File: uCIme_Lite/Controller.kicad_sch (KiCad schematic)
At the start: 36 parts, among them J11 SERIAL_MODE, J12 SERIAL_VOLTAGE_SELECT, Q5 BSS138, Q6 BSS138, Q7 BSS138, Q8 BSS138, U3 AP2204K-ADJ, U4 AP2204K-ADJ, U5 FT230XS, U6 TXB0104D

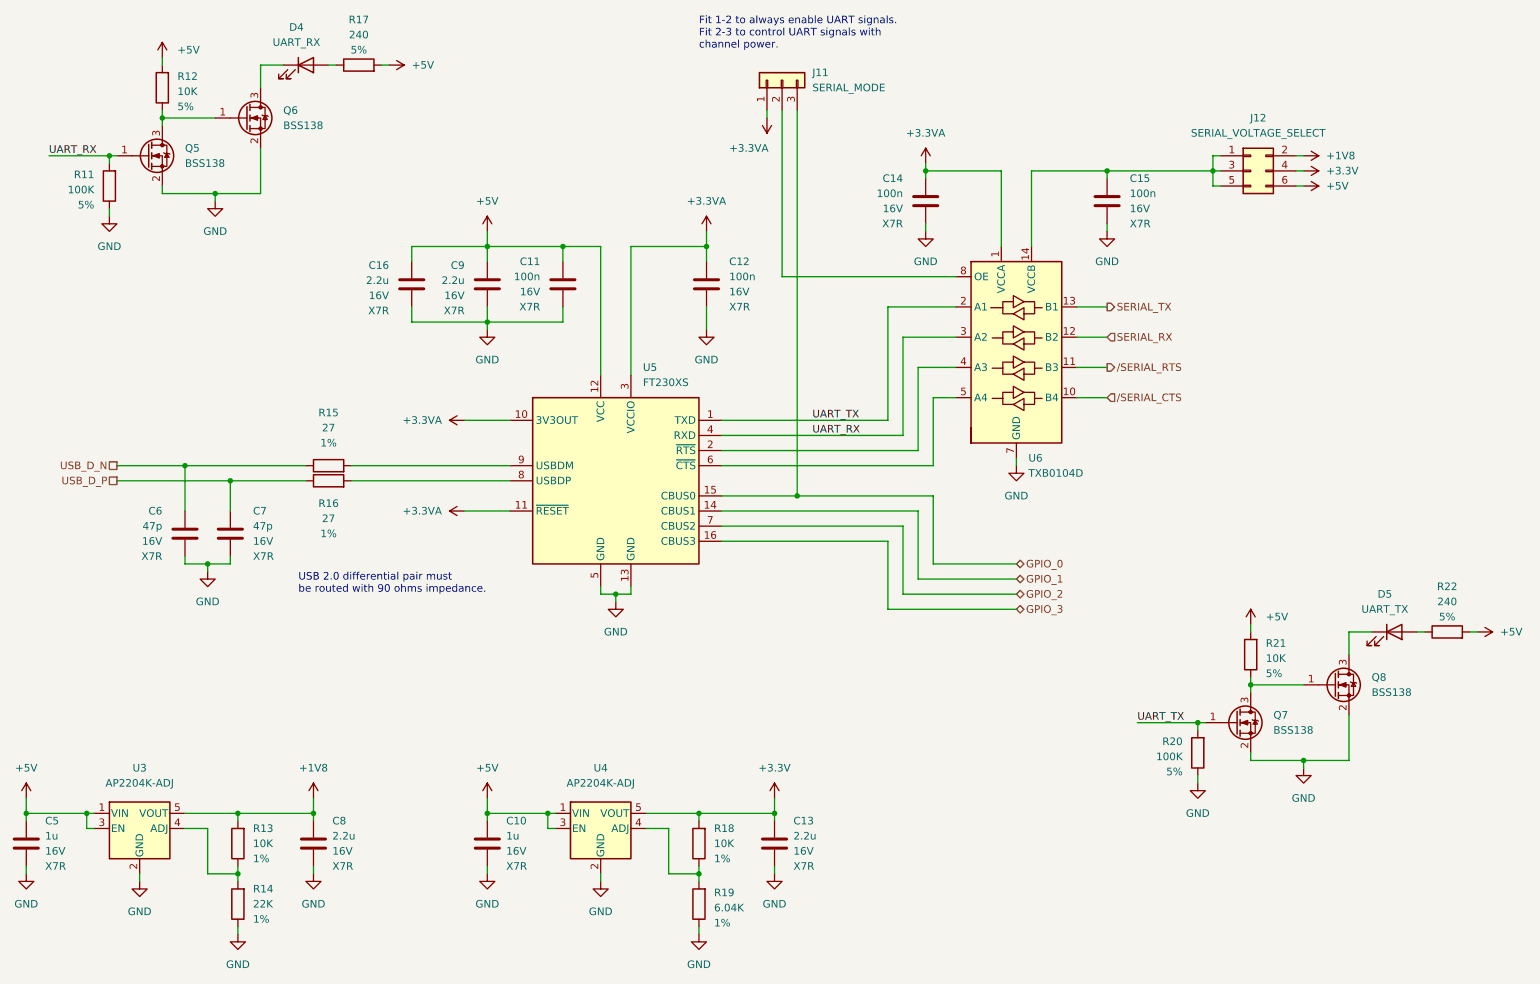
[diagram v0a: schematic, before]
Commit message: lite: Swapped UART RX and UART TX leds in schematic to ease PCB routing.
Signed-off-by: Adrien Ricciardi <aricciardi@baylibre.com>
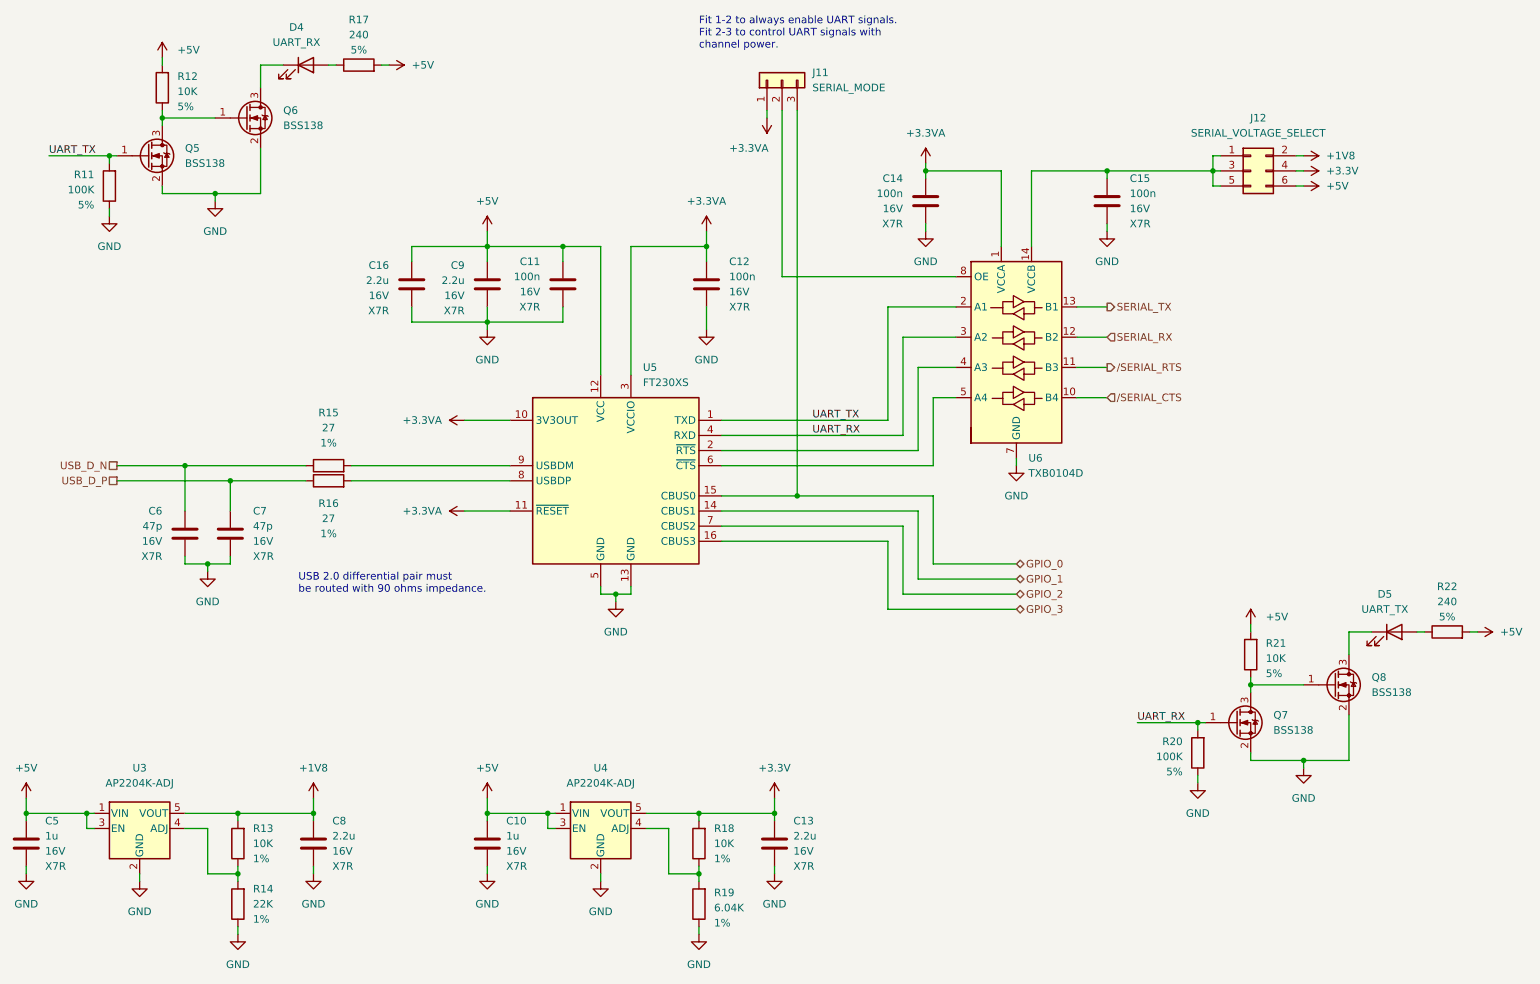
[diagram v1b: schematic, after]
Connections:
- net UART_RX: now also Q7.1 (G), R20.2; no longer Q5.1 (G), R11.2
- net UART_TX: now also Q5.1 (G), R11.2; no longer Q7.1 (G), R20.2
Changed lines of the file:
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@@
     (effects (font (size 1.27 1.27)) (justify left bottom))
   )
-  (label "UART_RX" (at 30.48 49.53 0) (fields_autoplaced)
+  (label "UART_TX" (at 30.48 49.53 0) (fields_autoplaced)
     (effects (font (size 1.27 1.27)) (justify left bottom))
   )
@@
     (effects (font (size 1.27 1.27)) (justify left bottom))
   )
-  (label "UART_TX" (at 213.36 144.78 0) (fields_autoplaced)
+  (label "UART_RX" (at 213.36 144.78 0) (fields_autoplaced)
     (effects (font (size 1.27 1.27)) (justify left bottom))
   )

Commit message: lite: Added Aisler part number properties in both schematic and PCB.
Signed-off-by: Adrien Ricciardi <aricciardi@baylibre.com>
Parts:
- C10, C5: AISLER_MPN (none) -> 1u 16V X7R 0603
- C11, C12, C14, C15: AISLER_MPN (none) -> 100n 16V X7R 0603
- C13, C16, C8, C9: AISLER_MPN (none) -> 2.2u 16V X7R 0603
- C6, C7: AISLER_MPN (none) -> 47p 16V X7R 0603
- D4, D5: AISLER_MPN (none) -> 150080SS75000
- Q5, Q6, Q7, Q8: AISLER_MPN (none) -> BSS138P,215
- R11, R20: AISLER_MPN (none) -> 100K 5% 0603
- R12, R13, R18, R21: AISLER_MPN (none) -> 10K 1% 0603
- R14: AISLER_MPN (none) -> 22K 1% 0603
- R15, R16: AISLER_MPN (none) -> 27 1% 0603
- R17, R22: AISLER_MPN (none) -> 240 5% 1206
- R19: AISLER_MPN (none) -> 6.04K 1% 0603
- U3, U4: AISLER_MPN (none) -> AP2204K-ADJTRG1
- U5: AISLER_MPN (none) -> FT230XS-R
- U6: AISLER_MPN (none) -> TXB0104DR
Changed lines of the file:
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@@
+      (effects (font (size 1.27 1.27)) hide)
+    )
+    (property "AISLER_MPN" "2.2u 16V X7R 0603" (at 152.4 165.1 0)
       (effects (font (size 1.27 1.27)) hide)
     )
@@
     )
     (property "PartNumber" "TXB0104DR" (at 193.04 82.55 0)
+      (effects (font (size 1.27 1.27)) hide)
+    )
+    (property "AISLER_MPN" "TXB0104DR" (at 193.04 82.55 0)
       (effects (font (size 1.27 1.27)) hide)
     )
@@
       (effects (font (size 1.27 1.27)) hide)
     )
+    (property "AISLER_MPN" "22K 1% 0603" (at 62.23 175.26 0)
+      (effects (font (size 1.27 1.27)) hide)
+    )
     (pin "1")
     (pin "2")
@@
     )
     (property "PartNumber" "CL10B104KO8NNNC" (at 208.28 57.15 0)
+      (effects (font (size 1.27 1.27)) hide)
+    )
+    (property "AISLER_MPN" "100n 16V X7R 0603" (at 208.28 57.15 0)
       (effects (font (size 1.27 1.27)) hide)
     )
@@
       (effects (font (size 1.27 1.27)) hide)
     )
+    (property "AISLER_MPN" "BSS138P,215" (at 63.5 43.18 0)
+      (effects (font (size 1.27 1.27)) hide)
+    )
     (pin "1")
     (pin "2")
@@
       (effects (font (size 1.27 1.27)) hide)
     )
+    (property "AISLER_MPN" "2.2u 16V X7R 0603" (at 74.93 165.1 0)
+      (effects (font (size 1.27 1.27)) hide)
+    )
     (pin "1")
     (pin "2")
@@
       (effects (font (size 1.27 1.27)) hide)
     )
+    (property "AISLER_MPN" "10K 1% 0603" (at 139.7 165.1 0)
+      (effects (font (size 1.27 1.27)) hide)
+    )
     (pin "1")
     (pin "2")
@@
       (effects (font (size 1.27 1.27)) hide)
     )
+    (property "AISLER_MPN" "47p 16V X7R 0603" (at 60.96 113.03 0)
+      (effects (font (size 1.27 1.27)) hide)
+    )
     (pin "1")
     (pin "2")
@@
     (property "Value2" "5%" (at 82.55 31.75 90)
       (effects (font (size 1.27 1.27)))
+    )
+    (property "AISLER_MPN" "240 5% 1206" (at 82.55 34.29 0)
+      (effects (font (size 1.27 1.27)) hide)
     )
     (pin "1")
@@
       (effects (font (size 1.27 1.27)) hide)
     )
+    (property "AISLER_MPN" "BSS138P,215" (at 229.87 144.78 0)
+      (effects (font (size 1.27 1.27)) hide)
+    )
     (pin "1")
     (pin "2")
@@
       (effects (font (size 1.27 1.27)) hide)
     )
+    (property "AISLER_MPN" "100n 16V X7R 0603" (at 177.8 57.15 0)
+      (effects (font (size 1.27 1.27)) hide)
+    )
     (pin "1")
     (pin "2")
@@
       (effects (font (size 1.27 1.27)) hide)
     )
+    (property "AISLER_MPN" "6.04K 1% 0603" (at 139.7 175.26 0)
+      (effects (font (size 1.27 1.27)) hide)
+    )
     (pin "1")
     (pin "2")
@@
     )
     (property "PartNumber" "AP2204K-ADJTRG1" (at 123.19 162.56 0)
+      (effects (font (size 1.27 1.27)) hide)
+    )
+    (property "AISLER_MPN" "AP2204K-ADJTRG1" (at 123.19 162.56 0)
       (effects (font (size 1.27 1.27)) hide)
     )
@@
       (effects (font (size 1.27 1.27)) hide)
     )
+    (property "AISLER_MPN" "27 1% 0603" (at 77.47 104.14 0)
+      (effects (font (size 1.27 1.27)) hide)
+    )
     (pin "1")
     (pin "2")
@@
       (effects (font (size 1.27 1.27)) hide)
     )
+    (property "AISLER_MPN" "100n 16V X7R 0603" (at 140.97 71.12 0)
+      (effects (font (size 1.27 1.27)) hide)
+    )
     (pin "1")
     (pin "2")
@@
     (property "Value2" "5%" (at 38.1 57.785 0)
       (effects (font (size 1.27 1.27)) (justify left))
+    )
+    (property "AISLER_MPN" "100K 5% 0603" (at 40.64 54.61 0)
+      (effects (font (size 1.27 1.27)) hide)
     )
     (pin "1")
@@
       (effects (font (size 1.27 1.27)) (justify right))
     )
+    (property "AISLER_MPN" "10K 1% 0603" (at 49.53 38.1 0)
+      (effects (font (size 1.27 1.27)) hide)
+    )
     (pin "1")
     (pin "2")
@@
       (effects (font (size 1.27 1.27)) hide)
     )
+    (property "AISLER_MPN" "47p 16V X7R 0603" (at 53.34 113.03 0)
+      (effects (font (size 1.27 1.27)) hide)
+    )
     (pin "1")
     (pin "2")
@@
     )
     (property "PartNumber" "AP2204K-ADJTRG1" (at 45.72 162.56 0)
+      (effects (font (size 1.27 1.27)) hide)
+    )
+    (property "AISLER_MPN" "AP2204K-ADJTRG1" (at 45.72 162.56 0)
       (effects (font (size 1.27 1.27)) hide)
     )
@@
       (effects (font (size 1.27 1.27)) hide)
     )
+    (property "AISLER_MPN" "BSS138P,215" (at 246.38 138.43 0)
+      (effects (font (size 1.27 1.27)) hide)
+    )
     (pin "1")
     (pin "2")
@@
       (effects (font (size 1.27 1.27)) hide)
     )
+    (property "AISLER_MPN" "27 1% 0603" (at 77.47 101.6 0)
+      (effects (font (size 1.27 1.27)) hide)
+    )
     (pin "1")
     (pin "2")
@@
       (effects (font (size 1.27 1.27)) hide)
     )
+    (property "AISLER_MPN" "150080SS75000" (at 256.54 129.54 0)
+      (effects (font (size 1.27 1.27)) hide)
+    )
     (pin "1")
     (pin "2")
@@
     )
     (property "PartNumber" "150080SS75000" (at 73.66 34.29 0)
+      (effects (font (size 1.27 1.27)) hide)
+    )
+    (property "AISLER_MPN" "150080SS75000" (at 73.66 34.29 0)
       (effects (font (size 1.27 1.27)) hide)
     )
@@
       (effects (font (size 1.27 1.27)) hide)
     )
+    (property "AISLER_MPN" "BSS138P,215" (at 46.99 49.53 0)
+      (effects (font (size 1.27 1.27)) hide)
+    )
     (pin "1")
     (pin "2")
@@
       (effects (font (size 1.27 1.27)) hide)
     )
+    (property "AISLER_MPN" "100n 16V X7R 0603" (at 116.84 71.12 0)
+      (effects (font (size 1.27 1.27)) hide)
+    )
     (pin "1")
     (pin "2")
@@
       (effects (font (size 1.27 1.27)) (justify right))
     )
+    (property "AISLER_MPN" "10K 1% 0603" (at 232.41 133.35 0)
+      (effects (font (size 1.27 1.27)) hide)
+    )
     (pin "1")
     (pin "2")
@@
       (effects (font (size 1.27 1.27)) (justify left))
     )
+    (property "AISLER_MPN" "100K 5% 0603" (at 223.52 149.86 0)
+      (effects (font (size 1.27 1.27)) hide)
+    )
     (pin "1")
     (pin "2")
@@
       (effects (font (size 1.27 1.27)) hide)
     )
+    (property "AISLER_MPN" "2.2u 16V X7R 0603" (at 104.14 71.12 0)
+      (effects (font (size 1.27 1.27)) hide)
+    )
     (pin "1")
     (pin "2")
@@
     )
     (property "PartNumber" "CL10A225KO8NNNC" (at 91.44 71.12 0)
+      (effects (font (size 1.27 1.27)) hide)
+    )
+    (property "AISLER_MPN" "2.2u 16V X7R 0603" (at 91.44 71.12 0)
       (effects (font (size 1.27 1.27)) hide)
     )
@@
     )
     (property "PartNumber" "FT230XS-R" (at 125.73 104.14 0)
+      (effects (font (size 1.27 1.27)) hide)
+    )
+    (property "AISLER_MPN" "FT230XS-R" (at 125.73 104.14 0)
       (effects (font (size 1.27 1.27)) hide)
     )
@@
       (effects (font (size 1.27 1.27)) hide)
     )
+    (property "AISLER_MPN" "1u 16V X7R 0603" (at 26.67 165.1 0)
+      (effects (font (size 1.27 1.27)) hide)
+    )
     (pin "1")
     (pin "2")
@@
       (effects (font (size 1.27 1.27)) hide)
     )
+    (property "AISLER_MPN" "1u 16V X7R 0603" (at 104.14 165.1 0)
+      (effects (font (size 1.27 1.27)) hide)
+    )
     (pin "1")
     (pin "2")
@@
     )
     (property "PartNumber" "RNCP0603FTD10K0" (at 62.23 165.1 0)
+      (effects (font (size 1.27 1.27)) hide)
+    )
+    (property "AISLER_MPN" "10K 1% 0603" (at 62.23 165.1 0)
       (effects (font (size 1.27 1.27)) hide)
     )
@@
       (effects (font (size 1.27 1.27)))
     )
-    (pin "1")
+    (property "AISLER_MPN" "240 5% 1206" (at 265.43 129.54 0)
+      (effects (font (size 1.27 1.27)) hide)
+    )
+    (pin "1")

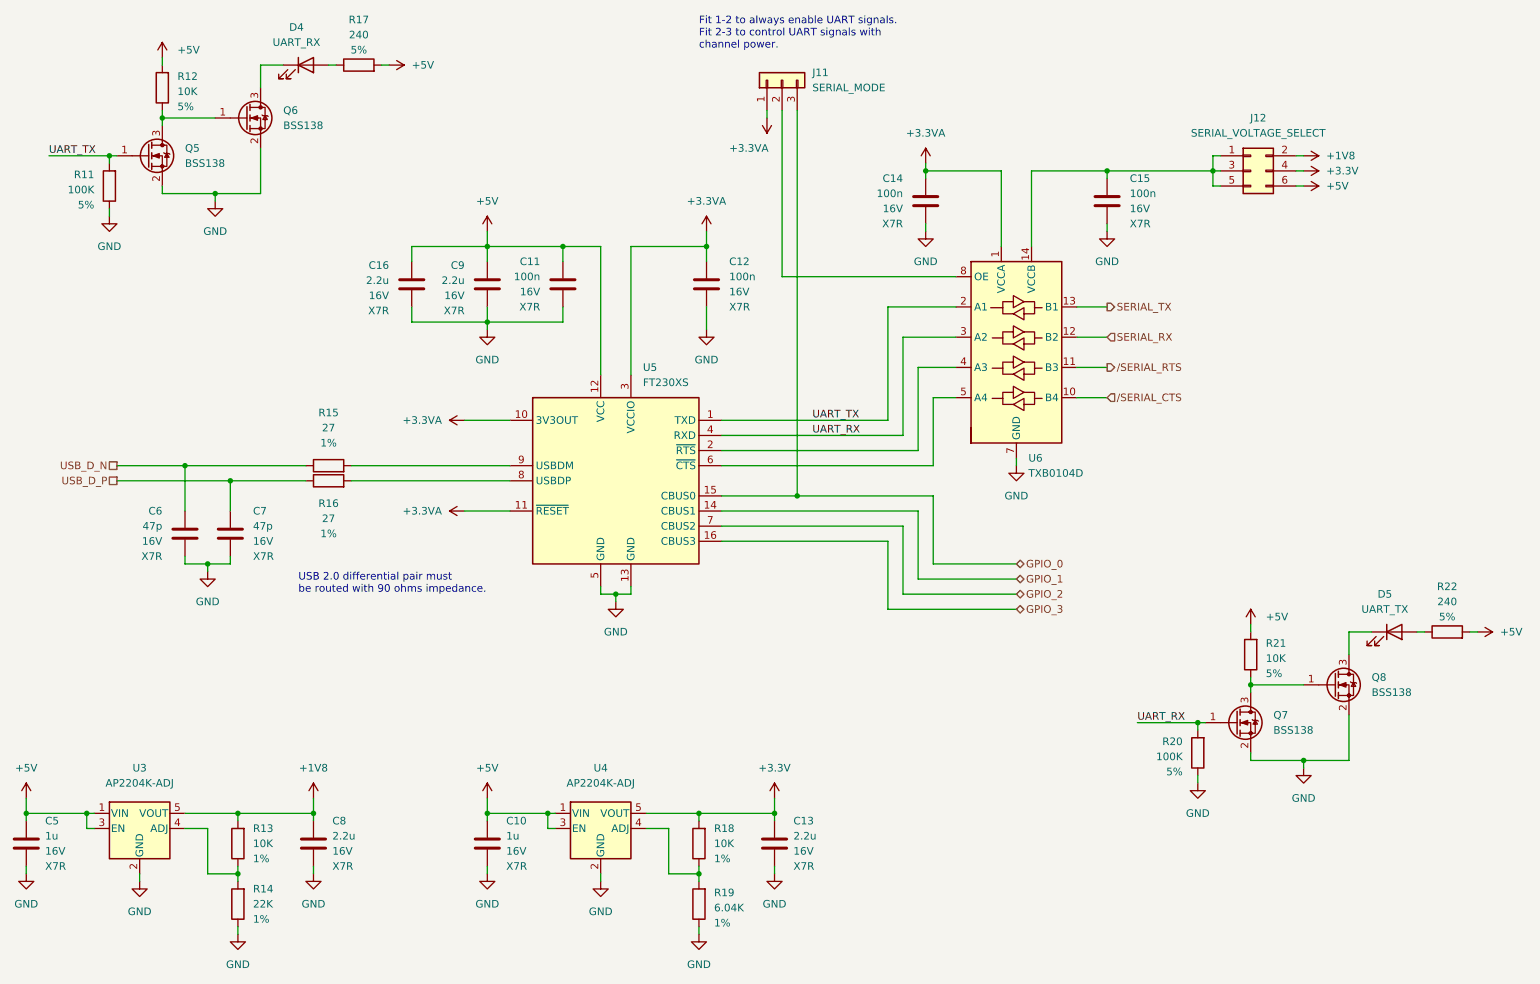
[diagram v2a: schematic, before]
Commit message: lite: Changed the serial RX and TX led names in schematic and PCB to match the previous change made to ease routing.
Signed-off-by: Adrien Ricciardi <aricciardi@baylibre.com>
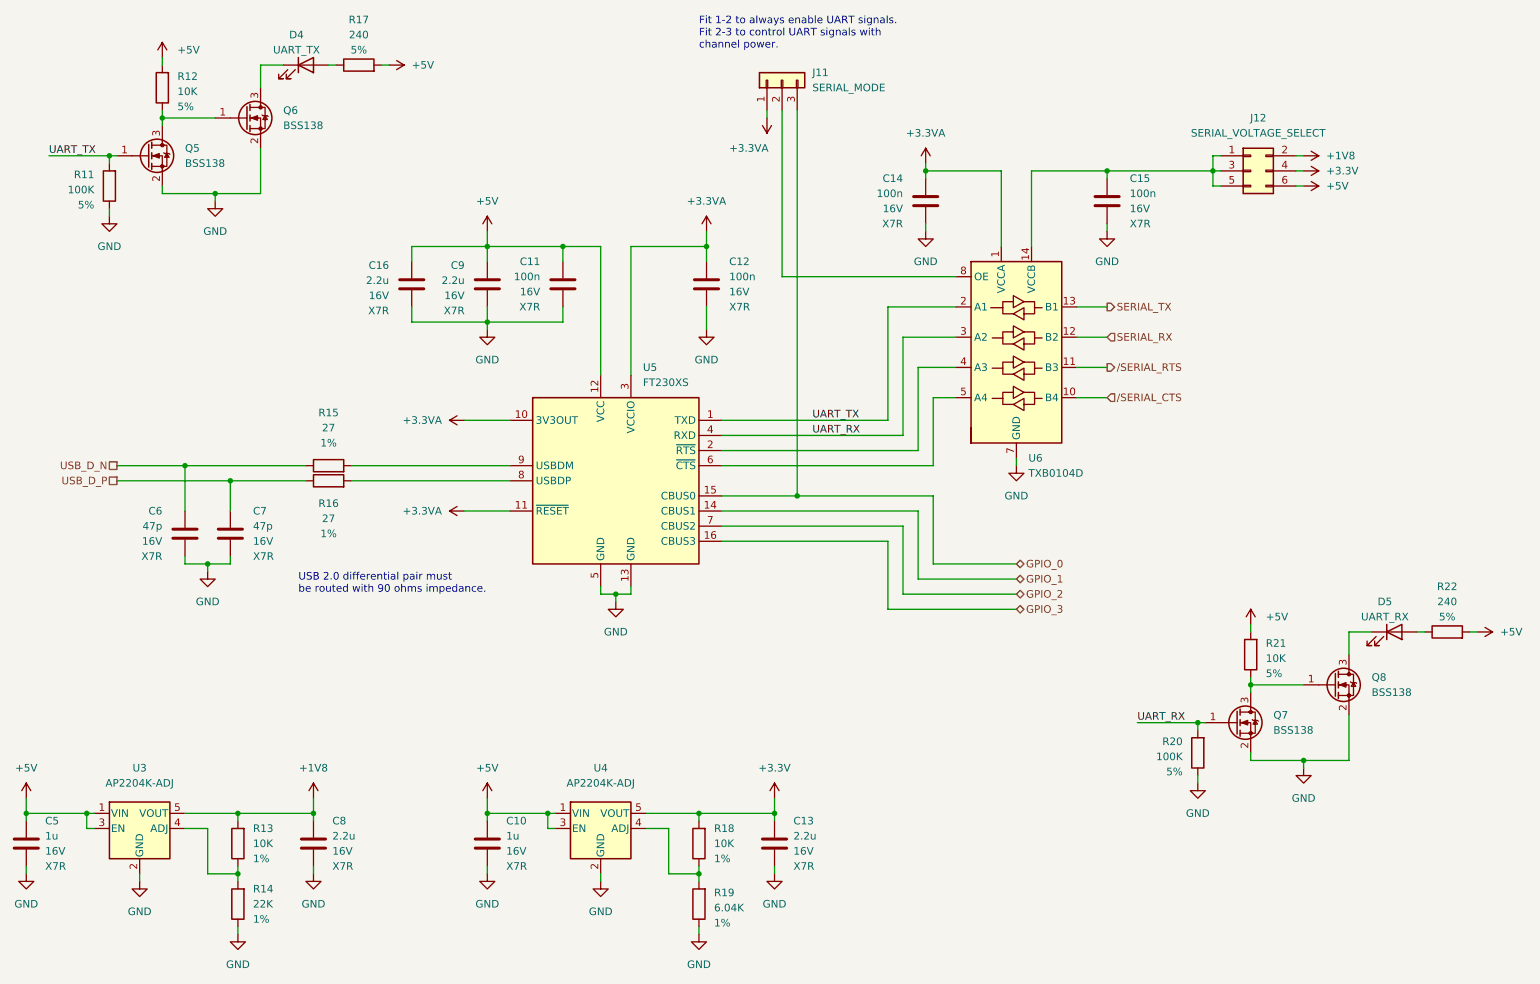
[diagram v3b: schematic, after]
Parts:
- D4: value UART_RX -> UART_TX
- D5: value UART_TX -> UART_RX
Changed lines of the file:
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@@
   (symbol (lib_id "Device:LED") (at 256.54 129.54 0) (unit 1)
     (in_bom yes) (on_board yes) (dnp no) (fields_autoplaced)
-    (property "Reference" "D5" (at 254.9525 123.19 0)
+    (property "Reference" "D5" (at 254.9525 124.46 0)
       (effects (font (size 1.27 1.27)))
     )
-    (property "Value" "UART_TX" (at 254.9525 125.73 0)
+    (property "Value" "UART_RX" (at 254.9525 127 0)
       (effects (font (size 1.27 1.27)))
     )
@@
   (symbol (lib_id "Device:LED") (at 73.66 34.29 0) (unit 1)
     (in_bom yes) (on_board yes) (dnp no) (fields_autoplaced)
-    (property "Reference" "D4" (at 72.0725 27.94 0)
+    (property "Reference" "D4" (at 72.0725 29.21 0)
       (effects (font (size 1.27 1.27)))
     )
-    (property "Value" "UART_RX" (at 72.0725 30.48 0)
+    (property "Value" "UART_TX" (at 72.0725 31.75 0)
       (effects (font (size 1.27 1.27)))
     )
